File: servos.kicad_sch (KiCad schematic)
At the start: 8 parts

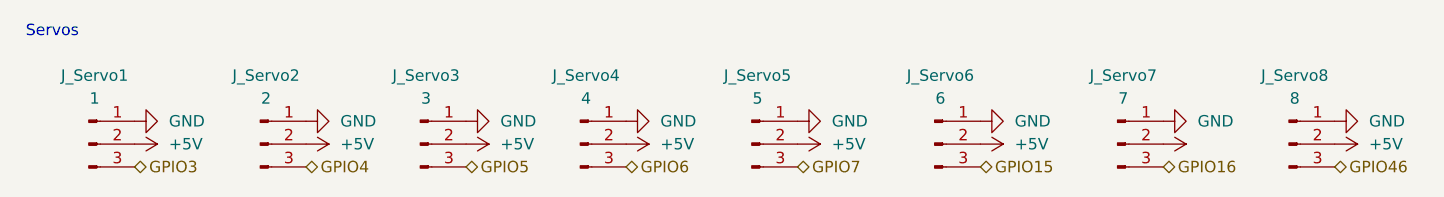
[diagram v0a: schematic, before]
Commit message: Updated to v1.1 to fix issues
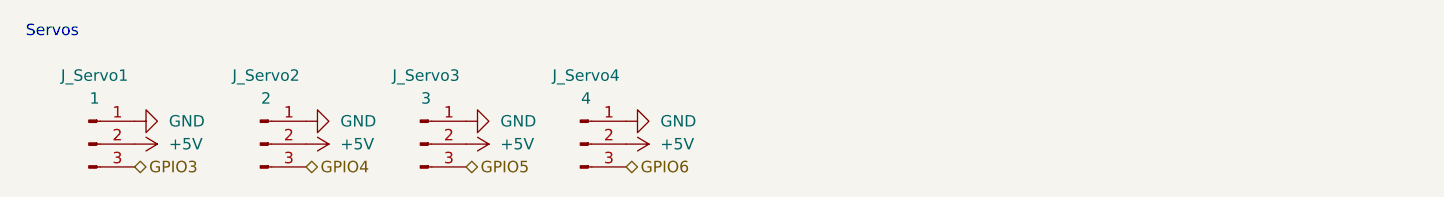
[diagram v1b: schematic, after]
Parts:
- removed J_Servo5: 5, Connector_PinHeader_2.54mm:PinHeader_1x03_P2.54mm_Vertical, symbol Connector:Conn_01x03_Pin
- removed J_Servo6: 6, Connector_PinHeader_2.54mm:PinHeader_1x03_P2.54mm_Vertical, symbol Connector:Conn_01x03_Pin
- removed J_Servo7: 7, Connector_PinHeader_2.54mm:PinHeader_1x03_P2.54mm_Vertical, symbol Connector:Conn_01x03_Pin
- removed J_Servo8: 8, Connector_PinHeader_2.54mm:PinHeader_1x03_P2.54mm_Vertical, symbol Connector:Conn_01x03_Pin
